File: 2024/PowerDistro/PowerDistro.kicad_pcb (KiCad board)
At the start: 2 copper layers, 1 part

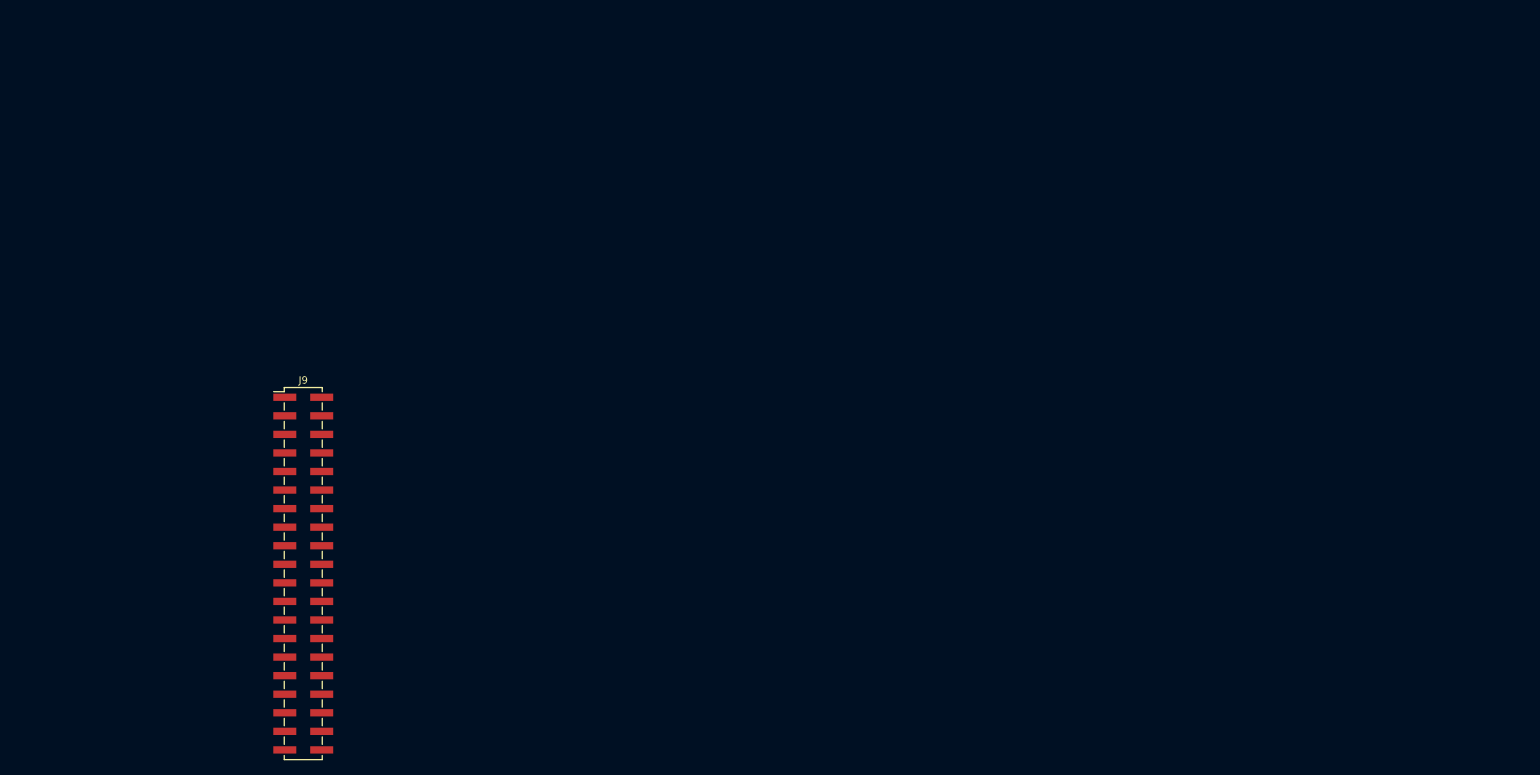
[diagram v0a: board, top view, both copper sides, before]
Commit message: placed the footprints onto the power distro PCB and started placement
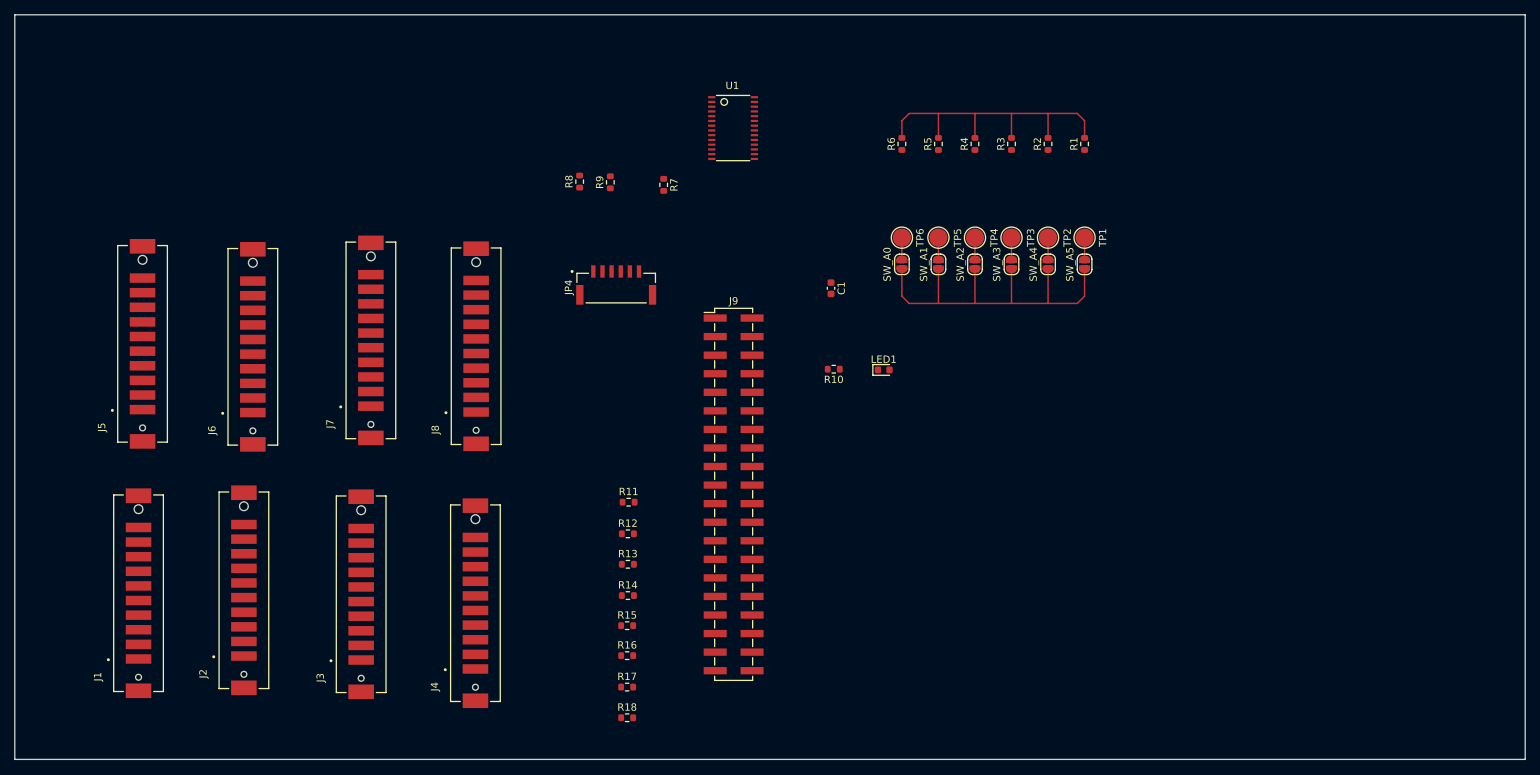
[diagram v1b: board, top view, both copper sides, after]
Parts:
- added C1: 10uF, Capacitor_SMD:C_0603_1608Metric, F.Cu at (129.8, 55.9)
- added J1: AMPHENOL_10159560-A00221RLF, PowerDistroFootprints:AMPHENOL_10159560-A00221RLF, F.Cu at (35.0, 97.7)
- added J2: AMPHENOL_10159560-A00221RLF, PowerDistroFootprints:AMPHENOL_10159560-A00221RLF, F.Cu at (49.5, 97.3)
- added J3: AMPHENOL_10159560-A00221RLF, PowerDistroFootprints:AMPHENOL_10159560-A00221RLF, F.Cu at (65.5, 97.8)
- added J4: AMPHENOL_10159560-A00221RLF, PowerDistroFootprints:AMPHENOL_10159560-A00221RLF, F.Cu at (81.1, 99.0)
- added J5: AMPHENOL_10159560-A00221RLF, PowerDistroFootprints:AMPHENOL_10159560-A00221RLF, F.Cu at (35.6, 63.5)
- added J6: AMPHENOL_10159560-A00221RLF, PowerDistroFootprints:AMPHENOL_10159560-A00221RLF, F.Cu at (50.7, 63.9)
- added J7: AMPHENOL_10159560-A00221RLF, PowerDistroFootprints:AMPHENOL_10159560-A00221RLF, F.Cu at (66.8, 63.1)
- added J8: AMPHENOL_10159560-A00221RLF, PowerDistroFootprints:AMPHENOL_10159560-A00221RLF, F.Cu at (81.2, 63.9)
- added JP4: JST_SM06B-GHS-TB_LF__SN_, PowerDistroFootprints:JST_SM06B-GHS-TB_LF__SN_, F.Cu at (100.4, 55.5)
- added LED1: GREEN, LED_SMD:LED_0603_1608Metric, F.Cu at (137.0, 67.1)
- added R1: 10k, Resistor_SMD:R_0603_1608Metric, F.Cu at (164.5, 36.2)
- added R10: 470, Resistor_SMD:R_0603_1608Metric, F.Cu at (130.2, 67.0)
- added R11: 220, Resistor_SMD:R_0603_1608Metric, F.Cu at (102.1, 85.2)
- added R12: 220, Resistor_SMD:R_0603_1608Metric, F.Cu at (102.0, 89.5)
- added R13: 220, Resistor_SMD:R_0603_1608Metric, F.Cu at (102.0, 93.7)
- added R14: 220, Resistor_SMD:R_0603_1608Metric, F.Cu at (102.0, 98.0)
- added R15: 220, Resistor_SMD:R_0603_1608Metric, F.Cu at (101.9, 102.1)
- added R16: 220, Resistor_SMD:R_0603_1608Metric, F.Cu at (101.9, 106.2)
- added R17: 220, Resistor_SMD:R_0603_1608Metric, F.Cu at (101.9, 110.5)
- added R18: 220, Resistor_SMD:R_0603_1608Metric, F.Cu at (101.9, 114.7)
- added R2: 10k, Resistor_SMD:R_0603_1608Metric, F.Cu at (159.5, 36.2)
- added R3: 10k, Resistor_SMD:R_0603_1608Metric, F.Cu at (154.5, 36.2)
- added R4: 10k, Resistor_SMD:R_0603_1608Metric, F.Cu at (149.5, 36.2)
- added R5: 10k, Resistor_SMD:R_0603_1608Metric, F.Cu at (144.5, 36.2)
- added R6: 10k, Resistor_SMD:R_0603_1608Metric, F.Cu at (139.5, 36.2)
- added R7: 10k, Resistor_SMD:R_0603_1608Metric, F.Cu at (106.9, 41.8)
- added R8: 10k, Resistor_SMD:R_0603_1608Metric, F.Cu at (95.4, 41.3)
- added R9: 10k, Resistor_SMD:R_0603_1608Metric, F.Cu at (99.6, 41.4)
- added SW_A0: SolderJumper_2_Open, Jumper:SolderJumper-2_P1.3mm_Open_RoundedPad1.0x1.5mm, F.Cu at (139.5, 52.6)
- added SW_A1: SolderJumper_2_Open, Jumper:SolderJumper-2_P1.3mm_Open_RoundedPad1.0x1.5mm, F.Cu at (144.5, 52.6)
- added SW_A2: SolderJumper_2_Open, Jumper:SolderJumper-2_P1.3mm_Open_RoundedPad1.0x1.5mm, F.Cu at (149.5, 52.6)
- added SW_A3: SolderJumper_2_Open, Jumper:SolderJumper-2_P1.3mm_Open_RoundedPad1.0x1.5mm, F.Cu at (154.5, 52.6)
- added SW_A4: SolderJumper_2_Open, Jumper:SolderJumper-2_P1.3mm_Open_RoundedPad1.0x1.5mm, F.Cu at (159.5, 52.6)
- added SW_A5: SolderJumper_2_Open, Jumper:SolderJumper-2_P1.3mm_Open_RoundedPad1.0x1.5mm, F.Cu at (164.5, 52.6)
- added TP1: TestPoint, TestPoint:TestPoint_Pad_D2.5mm, F.Cu at (164.5, 49.0)
- added TP2: TestPoint, TestPoint:TestPoint_Pad_D2.5mm, F.Cu at (159.5, 49.0)
- added TP3: TestPoint, TestPoint:TestPoint_Pad_D2.5mm, F.Cu at (154.5, 49.0)
- added TP4: TestPoint, TestPoint:TestPoint_Pad_D2.5mm, F.Cu at (149.5, 49.0)
- added TP5: TestPoint, TestPoint:TestPoint_Pad_D2.5mm, F.Cu at (144.5, 49.0)
- added TP6: TestPoint, TestPoint:TestPoint_Pad_D2.5mm, F.Cu at (139.5, 49.0)
- added U1: TSSOP28, PowerDistroFootprints:TSSOP28, F.Cu at (116.4, 34.0)
- moved J9 59.9 mm to (116.5, 84.1)
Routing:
- net VCC: track 0.00 -> 52.0 mm
- net GND: track 0.00 -> 43.9 mm
- net A5: track 0.00 -> 3.00 mm
- net A4: track 0.00 -> 3.00 mm
- net A3: track 0.00 -> 3.00 mm
- net A2: track 0.00 -> 3.00 mm
- net A1: track 0.00 -> 3.00 mm
- net A0: track 0.00 -> 3.00 mm
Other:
- board outline added: 206.7 x 101.9 mm

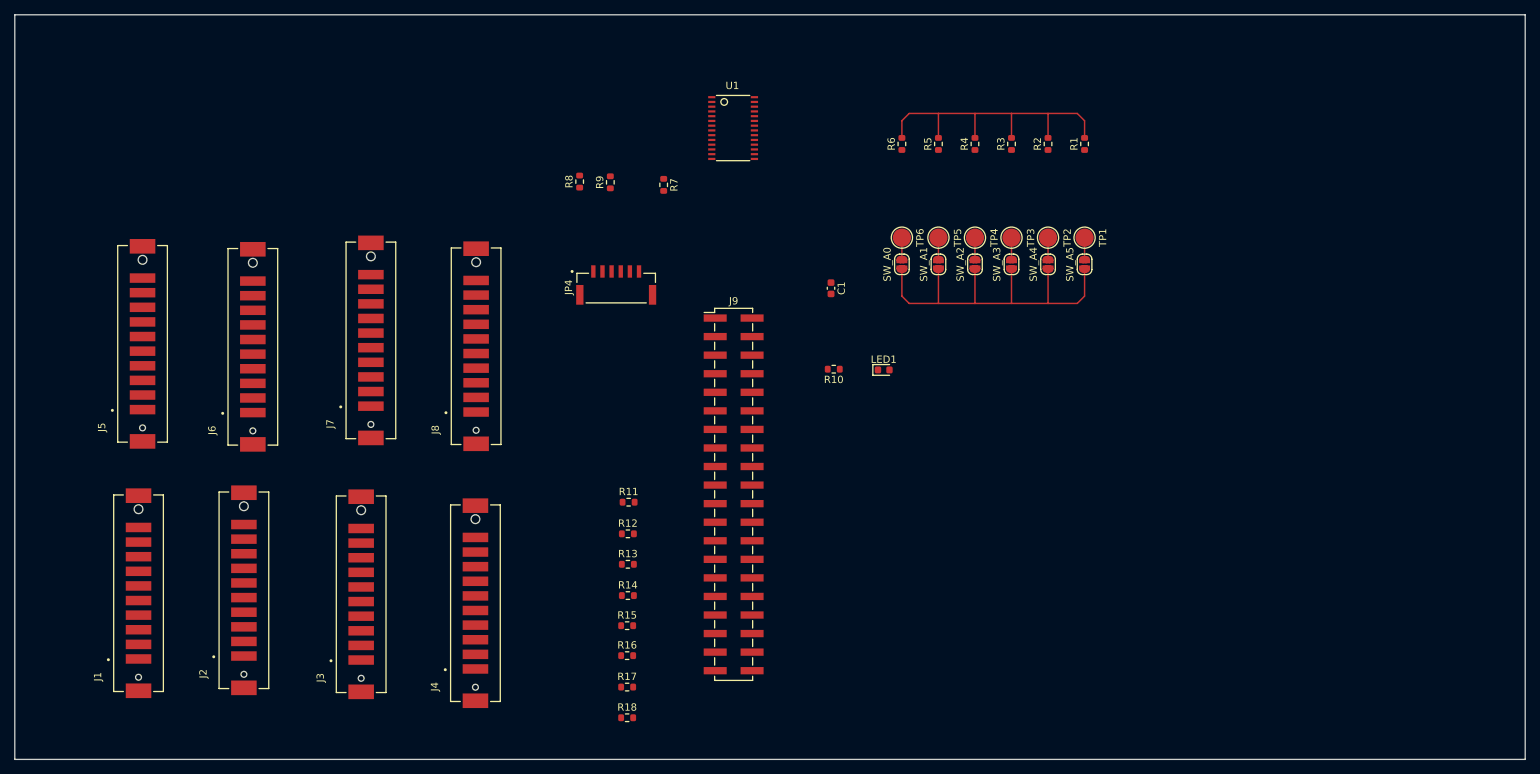
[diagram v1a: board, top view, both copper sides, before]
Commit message: changed PowerDistro PCB to 4 layers
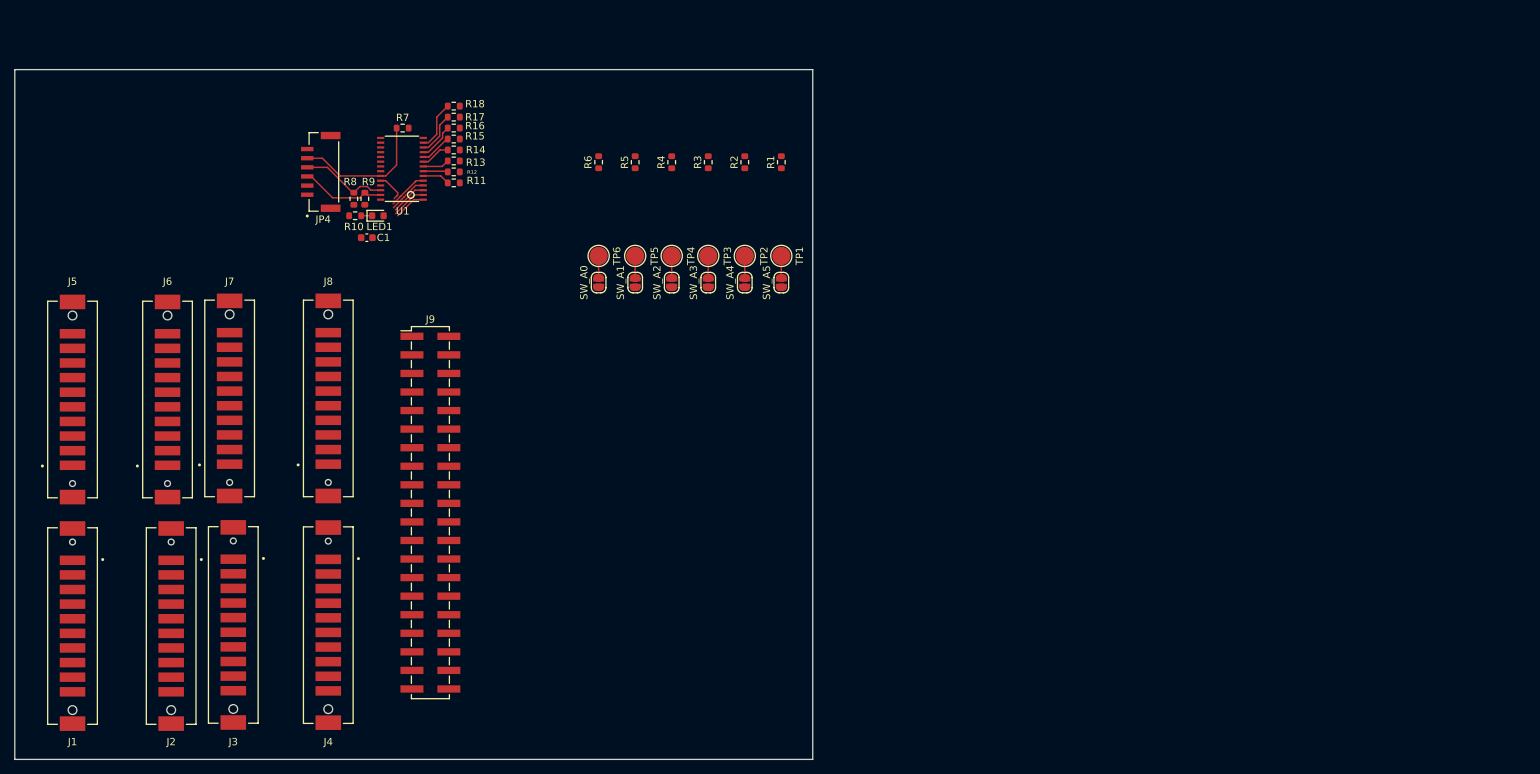
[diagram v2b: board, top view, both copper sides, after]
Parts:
- moved R18 87.0 mm to (78.2, 31.0), turned to 180 degrees
- moved R17 81.5 mm to (78.2, 32.5), turned to 180 degrees
- moved R16 76.0 mm to (78.2, 34.0), turned to 180 degrees
- moved LED1 72.4 mm to (67.8, 46.0)
- moved R15 70.7 mm to (78.2, 35.5), turned to 180 degrees
- moved R10 68.8 mm to (64.7, 46.0)
- moved R14 65.5 mm to (78.2, 37.0), turned to 180 degrees
- moved C1 63.9 mm to (66.3, 49.0), turned to 180 degrees
- moved R13 60.1 mm to (78.2, 38.5), turned to 180 degrees
- moved R12 55.0 mm to (78.2, 40.0), turned to 180 degrees
- moved R11 49.8 mm to (78.2, 41.5), turned to 180 degrees
- moved U1 45.7 mm to (71.1, 39.6), turned to 90 degrees
- moved JP4 43.3 mm to (60.0, 40.0), turned to 90 degrees
- moved J9 41.6 mm to (75.0, 86.6)
- moved R1 41.6 mm to (123.0, 38.7)
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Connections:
- J1 pad 3: (no net) -> GND
- J1 pad 5: (no net) -> GND
- J1 pad 7: (no net) -> GND
- J1 pad 9: (no net) -> GND
- JP4 pad 1: (no net) -> 5.0_VDC
- JP4 pad 2: (no net) -> VCC
- JP4 pad 3: (no net) -> SDA
- JP4 pad 4: (no net) -> SCL
- JP4 pad 5: (no net) -> OE
- JP4 pad 6: (no net) -> GND
- JP4 pad S1: (no net) -> GND
- JP4 pad S2: (no net) -> GND
- U1 pad 1: (no net) -> A0
- U1 pad 10: (no net) -> COM_5
- U1 pad 11: (no net) -> COM_6
- U1 pad 12: (no net) -> COM_7
- U1 pad 13: (no net) -> COM_8
- U1 pad 14: (no net) -> GND
- U1 pad 2: (no net) -> A1
- U1 pad 23: (no net) -> OE
- U1 pad 24: (no net) -> A5
- U1 pad 25: (no net) -> GND
- U1 pad 26: (no net) -> SCL
- U1 pad 27: (no net) -> SDA
- U1 pad 28: (no net) -> VCC
- U1 pad 3: (no net) -> A2
- U1 pad 4: (no net) -> A3
- U1 pad 5: (no net) -> A4
- U1 pad 6: (no net) -> COM_1
- U1 pad 7: (no net) -> COM_2
- U1 pad 8: (no net) -> COM_3
- U1 pad 9: (no net) -> COM_4
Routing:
- net VCC: track 52.0 -> 0.00 mm
- net GND: track 43.9 -> 0.55 mm
- net OE: track 0.00 -> 18.9 mm
- net SCL: track 0.00 -> 12.0 mm
- net SDA: track 0.00 -> 11.7 mm
- net COM_8: track 0.00 -> 6.79 mm
- net COM_7: track 0.00 -> 5.94 mm
- net A4: track 3.00 -> 8.44 mm
- net A3: track 3.00 -> 8.36 mm
- net COM_6: track 0.00 -> 5.10 mm
- net A2: track 3.00 -> 7.93 mm
- net A1: track 3.00 -> 7.85 mm
- net A0: track 3.00 -> 7.41 mm
- net COM_5: track 0.00 -> 4.36 mm
- net A5: track 3.00 -> 7.05 mm
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- added copper zone on In1.Cu, net 5.0_VDC
- added copper zone on In2.Cu, net GND
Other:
- board size 206.7 x 101.9 mm -> 109.2 x 94.4 mm
- copper layers 2 -> 4

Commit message: peters yelling me
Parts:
- moved R18 30.5 mm to (56.0, 52.0), turned to -90 degrees
- moved R17 27.7 mm to (58.5, 52.0), turned to -90 degrees
- moved R16 24.9 mm to (61.0, 52.0), turned to -90 degrees
- moved R15 22.1 mm to (63.5, 52.0), turned to -90 degrees
- moved R14 19.3 mm to (66.0, 52.0), turned to -90 degrees
- moved R13 16.6 mm to (68.5, 52.0), turned to -90 degrees
- moved R12 14.0 mm to (71.0, 52.0), turned to -90 degrees
- moved LED1 13.9 mm to (54.0, 44.3), turned to 90 degrees
- moved R11 11.5 mm to (73.5, 52.0), turned to -90 degrees
- moved R10 9.96 mm to (54.8, 47.5), turned to 0 degrees
- moved C1 3.27 mm to (68.0, 46.2), turned to -90 degrees
- moved R8 1.12 mm to (63.5, 44.2)
- moved JP4 1.00 mm to (59.0, 40.0)
- moved R7 0.50 mm to (71.2, 33.5)
- moved R9 0.50 mm to (66.0, 44.2)
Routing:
- net COM_8: track 6.79 -> 0.00 mm
- net COM_7: track 5.94 -> 0.00 mm
- net A4: track 8.44 -> 3.00 mm
- net A3: track 8.36 -> 3.00 mm
- net COM_6: track 5.10 -> 0.00 mm
- net A2: track 7.93 -> 3.00 mm
- net A1: track 7.85 -> 3.00 mm
- net A0: track 7.41 -> 3.00 mm
- net COM_5: track 4.36 -> 0.12 mm
- net A5: track 7.05 -> 3.00 mm
- net COM_4: track 4.01 -> 0.00 mm
- net COM_1: track 3.74 -> 0.00 mm
- net COM_3: track 3.66 -> 0.14 mm
- net COM_2: track 3.39 -> 0.00 mm
- net OE: track 18.9 -> 20.4 mm
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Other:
- board size 109.2 x 94.4 mm -> 235 x 285 mm

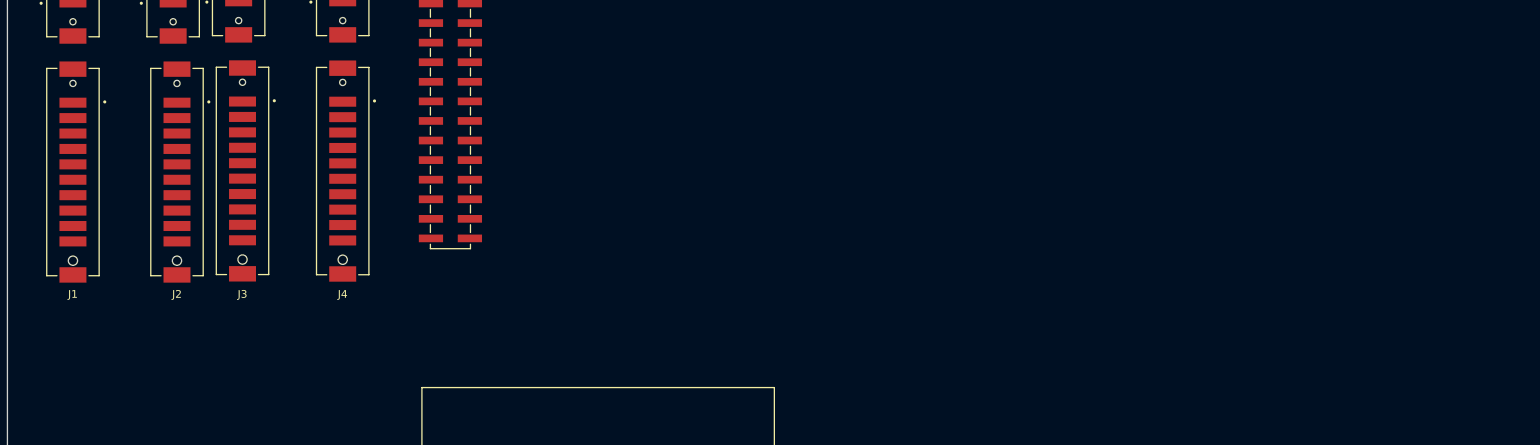
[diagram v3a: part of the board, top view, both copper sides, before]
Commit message: Added EASYBldc Outlines
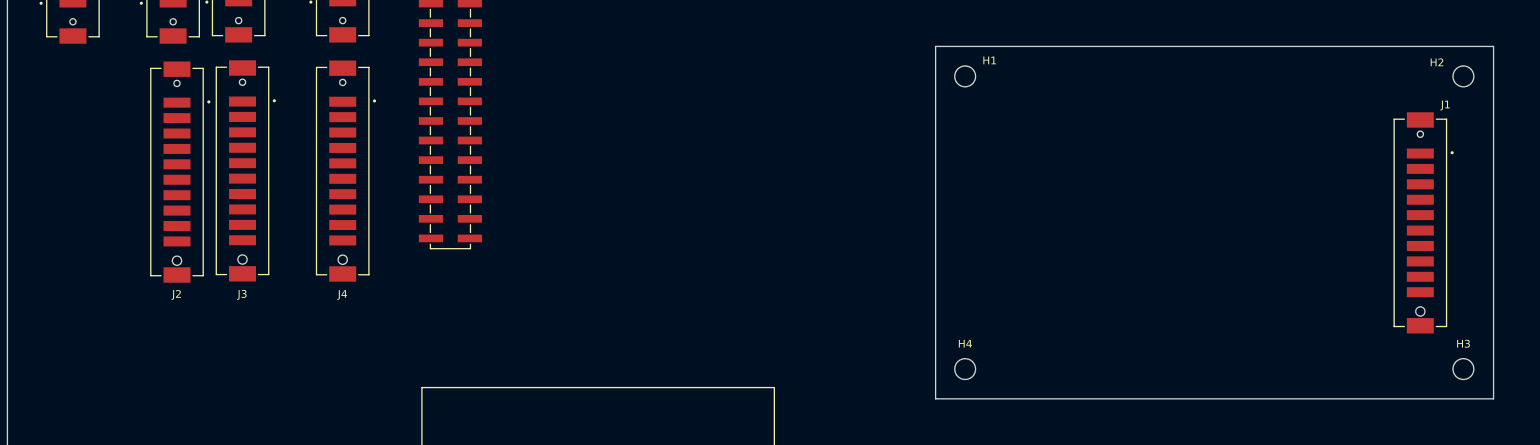
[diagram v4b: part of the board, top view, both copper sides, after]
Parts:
- added H1: M2.5, MountingHole:MountingHole_2.7mm_M2.5_ISO7380, F.Cu at (141.8, 89.7)
- added H2: M2.5, MountingHole:MountingHole_2.7mm_M2.5_ISO7380, F.Cu at (206.4, 89.7)
- added H3: M2.5, MountingHole:MountingHole_2.7mm_M2.5_ISO7380, F.Cu at (206.4, 127.7)
- added H4: M2.5, MountingHole:MountingHole_2.7mm_M2.5_ISO7380, F.Cu at (141.8, 127.7)
- J1: value AMPHENOL_10159560-A00221RLF -> 10159560-A00221RLF; footprint PowerDistroFootprints:AMPHENOL_10159560-A00221RLF -> EasyBLDC:AMPHENOL_10159560-A00221RLF
- moved J1 174.9 mm to (200.8, 108.7)
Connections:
- J1 pad S1: (no net) -> GND
- J1 pad S2: (no net) -> GND
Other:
- outline, holes or cut-outs redrawn
